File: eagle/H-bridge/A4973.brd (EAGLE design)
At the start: 63.6 x 45 mm, 13 parts, among them IC1 A4973DIL, X1 Load, X2 V_Load, X3 MODE

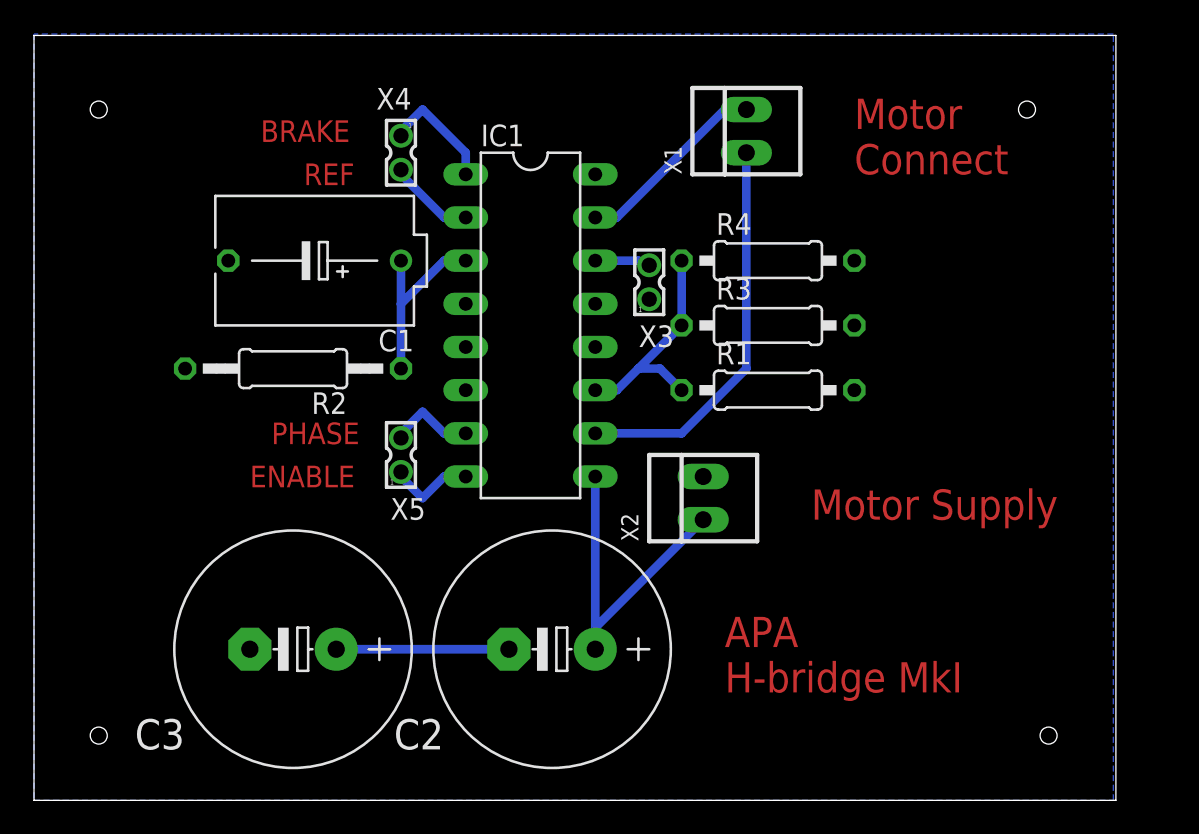
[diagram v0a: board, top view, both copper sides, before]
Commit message: Added 3.3 v to IC. Made one load pin floating
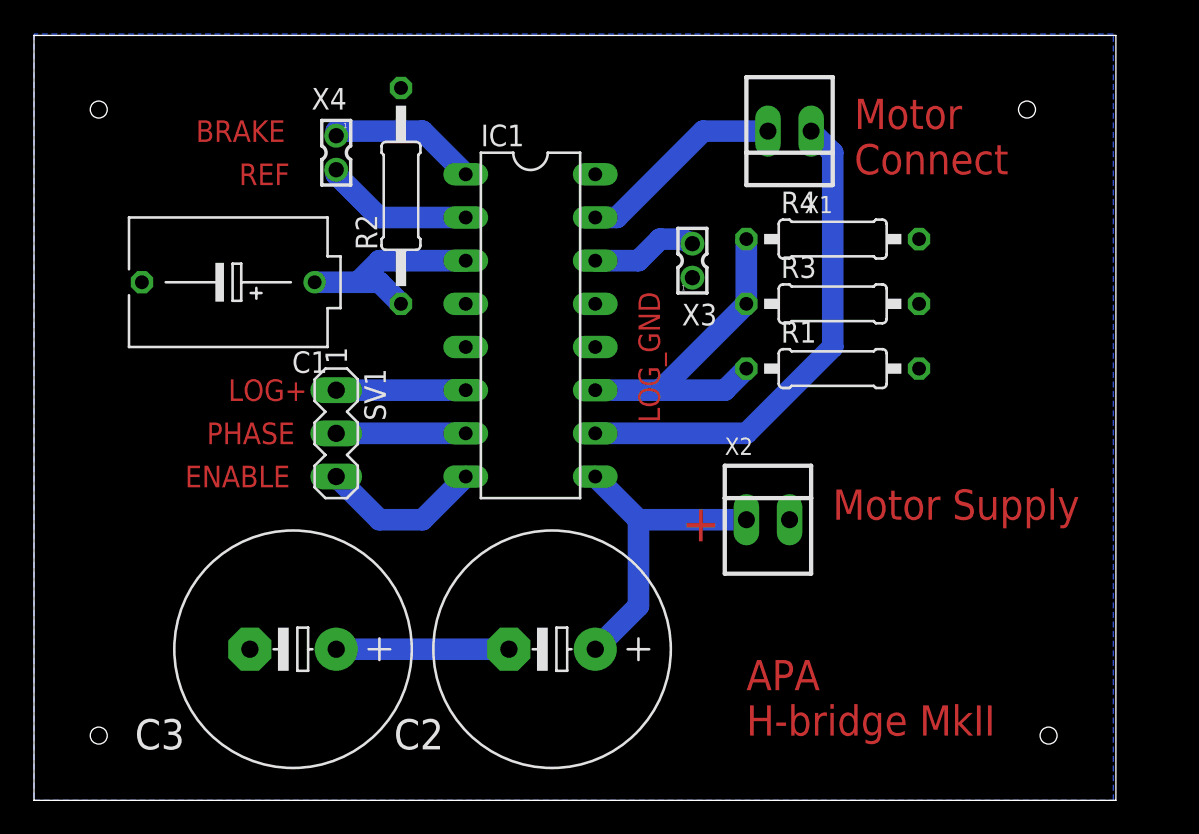
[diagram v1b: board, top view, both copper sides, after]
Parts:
- removed X5: (no value), con-garry:332-02
- added SV1: (no value), con-lstb:MA03-1
- moved R2 12.0 mm to (21.6, 35.6), turned to 90 degrees
- moved C1 5.24 mm to (11.4, 30.5)
- moved R4 4.02 mm to (47.0, 33.0)
- moved R1 4.02 mm to (47.0, 25.4)
- moved R3 4.02 mm to (47.0, 29.2)
- moved X2 4.02 mm to (43.2, 16.5), turned to 0 degrees
- moved X4 3.81 mm to (17.8, 38.1)
- moved X3 2.84 mm to (38.7, 31.8)
- moved X1 2.54 mm to (44.5, 39.4), turned to 180 degrees
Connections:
- net 3.3V: now also SV1.1
- net GND: no longer IC1.16
- net N$1: now also SV1.3; no longer X5.1
- net N$2: now also SV1.2; no longer X5.2
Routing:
- net 3.3V: track 0.00 -> 7.62 mm
- net N$6: track 13.5 -> 20.4 mm
- net N$4: track 23.2 -> 29.3 mm
- net N$1: track 5.13 -> 9.72 mm
- net N$10: track 5.13 -> 8.94 mm
- net MODE: track 3.23 -> 6.30 mm
- net N$2: track 5.13 -> 7.62 mm
- net N$9: track 6.93 -> 8.94 mm
- net N$7: track 11.2 -> 12.5 mm
- net N$5: track 11.5 -> 12.3 mm
- net N$8: track 19.1 -> 18.6 mm
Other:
- board text added: "+"
- board text added: "APA H-bridge MkII"
- board text added: "LOG+"
- board text added: "LOG_GND"
- board text removed: "APA H-bridge MkI"
